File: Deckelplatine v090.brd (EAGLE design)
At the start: 110 x 75 mm, 67 parts, among them IC1 MAX1487EESA+, IC2 74HCT595D, IC3 74HCT595D, IC4 74HCT595D, IC5 74HCT595D, IC6 74HCT595D, J1 52808-2570, Q1 BC846BSMD, Q2 BC846BSMD, U1 LM2676S, X1 236-404, X2 233-502

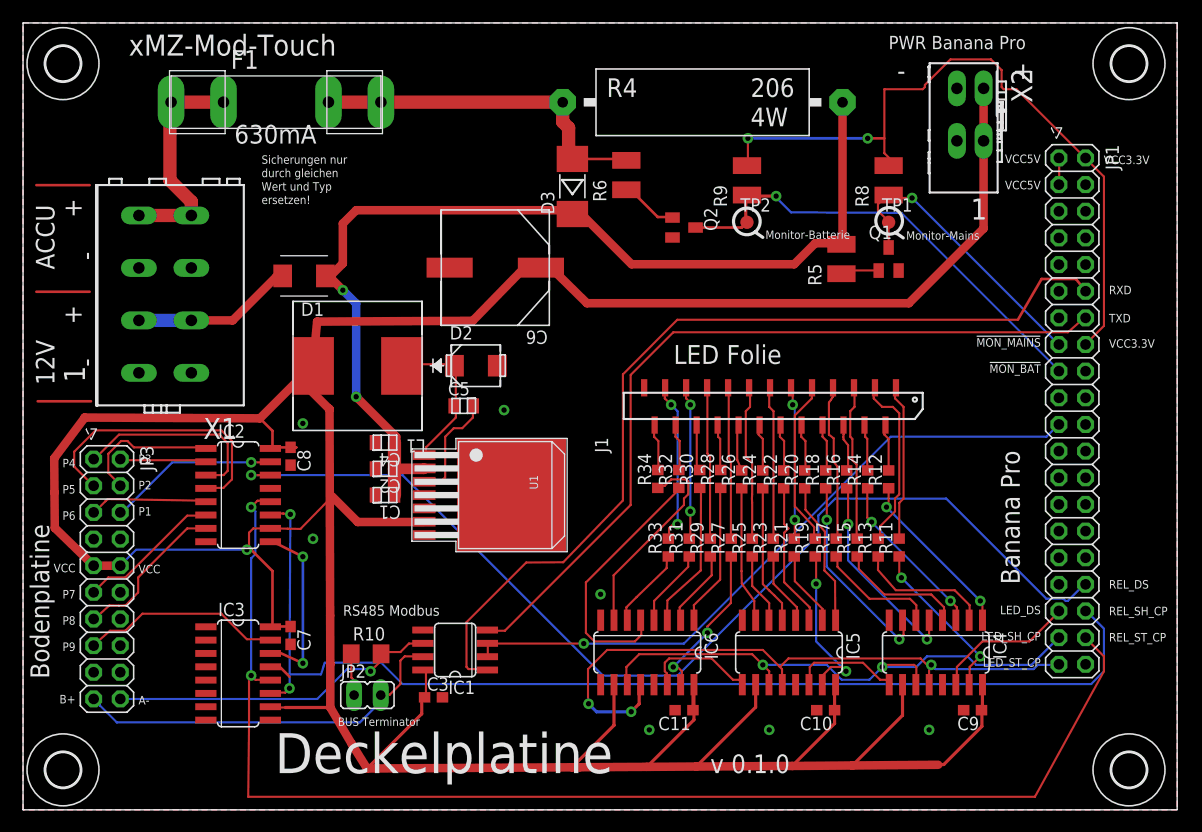
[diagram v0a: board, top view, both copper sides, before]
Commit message: Erste Version in der PCB Produktion (Conrad)
Dies ist die erste Produktion die über https://www.leiterplattenservice.com/
abgewickelt wurde.

https://www.leiterplattenservice.com/code/my_orderhistory_details.html?nr=CR558950f00063a

Details:
-------
Nachfolgend sehen Sie die Details der gewählten Bestellung CR558950f00063a. Die Bestellung erfolgte am 23.06.2015, 14:28:32.
Anzahl 	Beschreibung 	Netto
EUR 	Brutto
EUR
2 	PCB-POOL Prototyp doppelseitig 	134.50 	160.06

    Länge in mm: 75
    Breite in mm: 110
    Dateiname: xMZ_Mod_Touch_Deckelplatine_v0...
    Dateiformat: EAGLE
    Lieferzeit: 8 Arbeitstage (AT)
    Basismaterial: FR4, 35µmCu, 1,6mm
    Stopplack: ja
    Der Preis enthält die Kosten für den Stopplack in Höhe von 36.65 EUR
    Bestückungsdruck: ja, nur BS
    Der Preis enthält die Kosten für den Bestückungsdruck in Höhe von 18.32 EUR
    Oberfläche: chem. Nickel/Gold (ENIG) für superflache Pads
    Min. Leiterbahnstärke / -abstand: >= 0.125mm (5mil)
    Min. Bohrenddurchmesser: >= 0.2mm (8mil)
    Möchten Sie, dass wir Ihre Leiterplatte einem elektrischen Test unterziehen? ja
    Der Preis enthält die Kosten für den E-Test in Höhe von 25.87 EUR.

	Warenwert LEITERPLATTEN in EUR 	134.50 	160.06
	Versandkosten LEITERPLATTEN in EUR 	5.80 	6.90
	Gesamtsumme in EUR 	140.30 	166.96
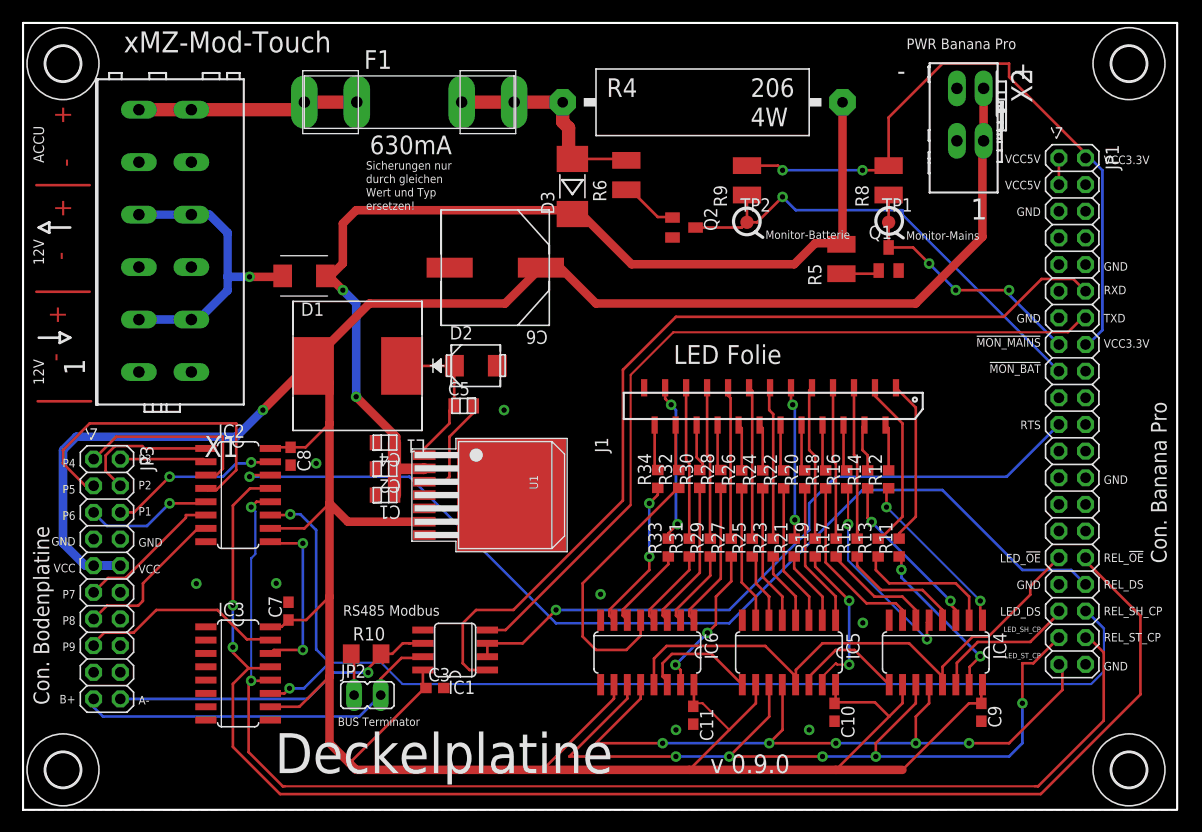
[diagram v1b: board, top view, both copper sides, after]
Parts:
- C10, C11, C7, C8, C9: value 100n -> 0.1uF
- C4: value 100.0 nF -> 0.1uF
- X1: value 236-404 -> 236-406/000-023; device con-wago_236:P-236-404 -> con-wago_236:P-236-406
- moved F1 12.7 mm to (36.8, 67.5)
- moved X1 5.08 mm to (14.0, 54.1)
- moved C7 2.33 mm to (25.3, 18.9), turned to 90 degrees
- moved C11 1.00 mm to (63.9, 9.02), turned to 270 degrees
- moved C3 0.90 mm to (39.3, 11.6)
- moved C10 0.87 mm to (77.3, 9.30), turned to 270 degrees
- moved C9 0.86 mm to (91.3, 9.30), turned to 270 degrees
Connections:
- removed net REL_SCK: IC2.11, IC3.11
- removed net REL_SER: IC2.14
- new net LED_!OE: IC4.13, IC5.13, IC6.13, JP1.31
- new net REL_!OE: IC2.13, IC3.13, JP1.32
- net 12V_VIN: now also X1.L4.1, X1.L4.2
- net ACCU+: now also X1.L6.1, X1.L6.2; no longer X1.L4.1, X1.L4.2
- net GND: now also X1.L5.1, X1.L5.2; no longer IC2.13, IC3.13, IC4.13, IC5.13, IC6.13
- net REL_DS: now also IC2.14
- net REL_SH_CP: now also IC2.11, IC3.11
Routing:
- net REL_!OE: track 0.00 -> 138.1 mm, vias 0 -> 2
- net REL_SH_CP: track 0.00 -> 106.7 mm, vias 0 -> 2
- net REL_SCK: track 106.7 -> 0.00 mm, vias 2 -> 0
- net REL_SER: track 102.0 -> 0.00 mm, vias 1 -> 0
- net REL_DS: track 0.00 -> 96.5 mm, vias 0 -> 1
- net LED_!OE: track 0.00 -> 53.8 mm
- net LED_SH_CP: track 54.1 -> 83.4 mm, vias 2 -> 5
- net VCC: track 356.5 -> 331.0 mm
- net 12V_VIN: track 112.6 -> 127.0 mm, vias 2 -> 3
- net ACCU+: track 55.1 -> 41.7 mm
- net LED_ST_CP: track 61.5 -> 68.7 mm, vias 3 -> 5
- net N$30: track 19.6 -> 14.7 mm, vias 0 -> 2
- net P5: track 26.8 -> 30.8 mm
- net VCC3.3V: track 67.8 -> 64.0 mm
- net !MON_MAINS: track 28.2 -> 25.3 mm, vias 1 -> 3
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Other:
- board text added: "Con. Banana Pro"
- board text added: "Con. Bodenplatine"
- board text added: "GND"
- board text added: "LED_!OE"
- board text added: "REL_!OE"
- board text added: "RTS"
- board text removed: "Banana Pro"
- board text removed: "Bodenplatine"
